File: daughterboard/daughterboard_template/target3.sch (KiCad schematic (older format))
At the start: 0 parts

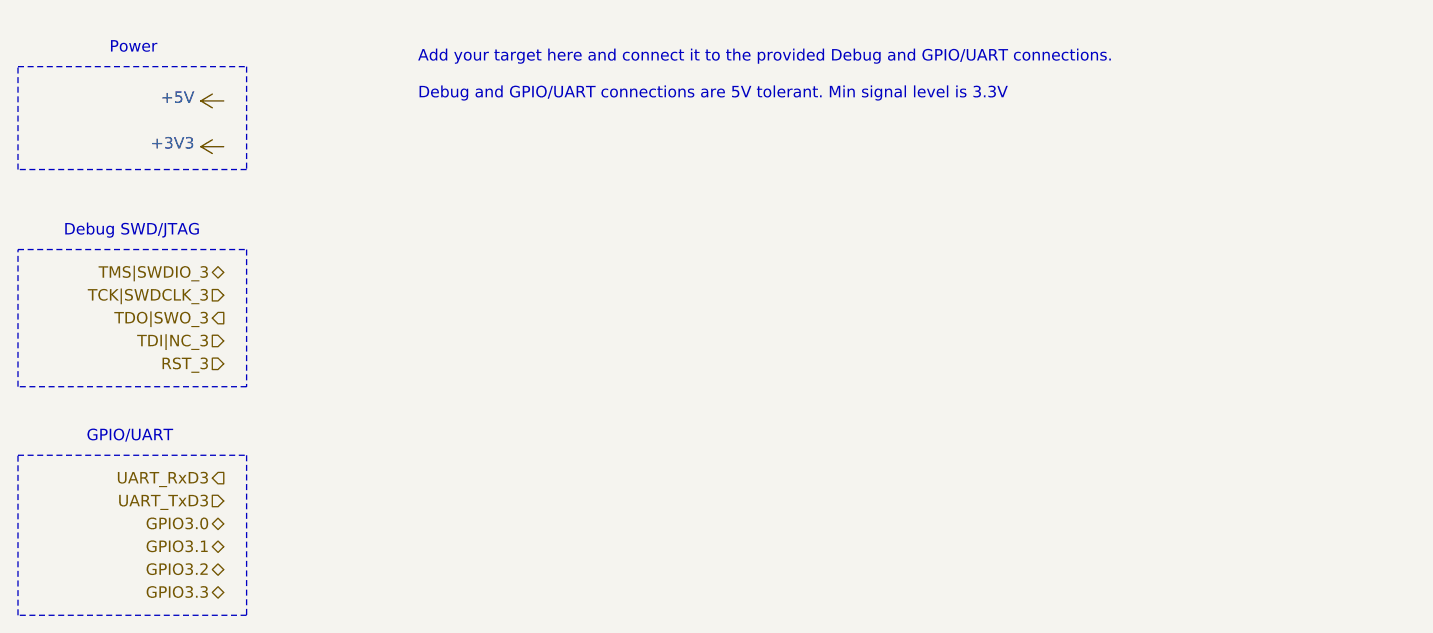
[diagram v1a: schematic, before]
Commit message: updated LED resistor values, updated partlists, minor change to daughterboard template
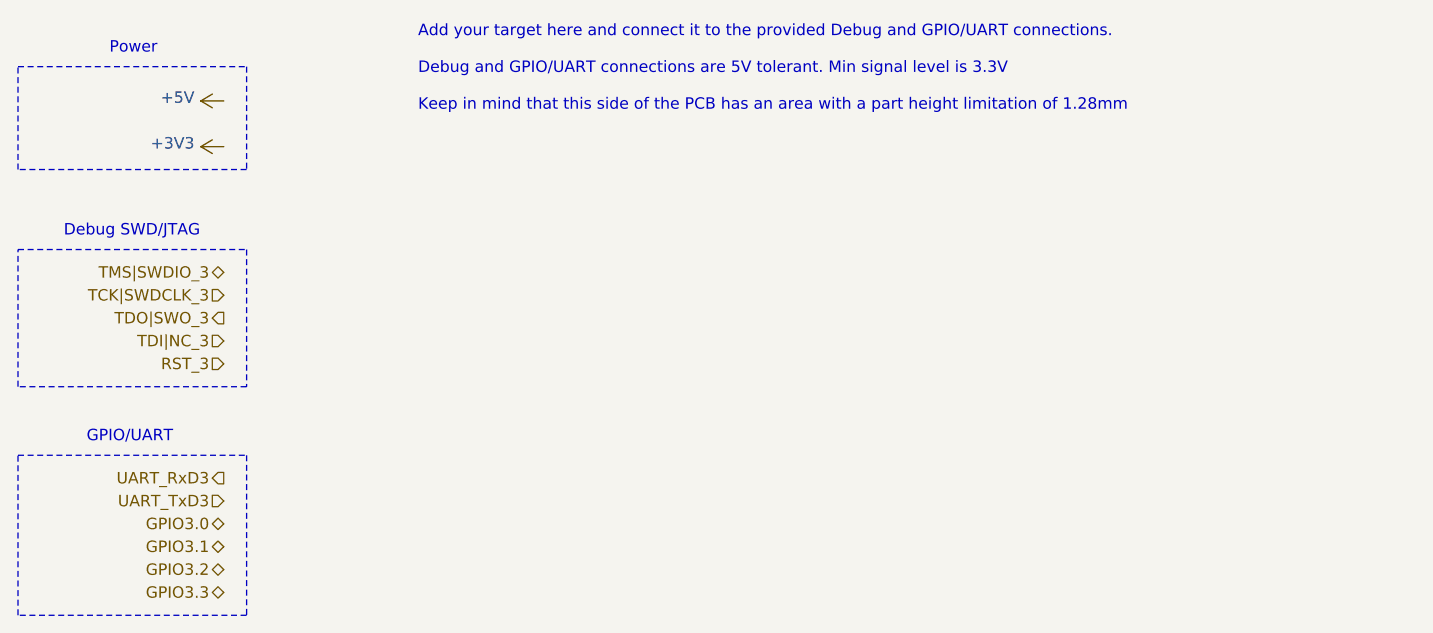
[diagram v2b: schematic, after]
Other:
- note added: "Add your target here and connect it to the provided Debug and GPIO/UART connections.\n\nDebug and GPIO/UART connections are 5V tolerant. Min signal level is 3.3V\n\nKeep in mind that this side of the PCB has an area with a part height limitation of 1.28mm"
- note removed: "Add your target here and connect it to the provided Debug and GPIO/UART connections.\n\nDebug and GPIO/UART connections are 5V tolerant. Min signal level is 3.3V"
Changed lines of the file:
@@
 Text Notes 1150 750  0    50   ~ 0
 Power
-Text Notes 2500 950  0    50   ~ 0
-Add your target here and connect it to the provided Debug and GPIO/UART connections.\n\nDebug and GPIO/UART connections are 5V tolerant. Min signal level is 3.3V
+Text Notes 2500 1000 0    50   ~ 0
+Add your target here and connect it to the provided Debug and GPIO/UART connections.\n\nDebug and GPIO/UART connections are 5V tolerant. Min signal level is 3.3V\n\nKeep in mind that this side of the PCB has an area with a part height limitation of 1.28mm
 $EndSCHEMATC
